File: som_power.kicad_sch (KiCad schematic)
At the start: 87 parts, among them J1 Hermaphroditic_Molex_203456-0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, Q10 DMG1012T-7, Q11 DMG1012T-7, Q17 DMG1012T-7, Q18 DMG1012T-7, Q20 DMG1012T-7, Q22 DMG1012T-7, Q7 DMG1012T-7, Q8 DMG1012T-7, SW2 SW_SPDT_PCM12SMTR, U70 MAX16150A_SOT, U72 TPS3840PL30DBVR

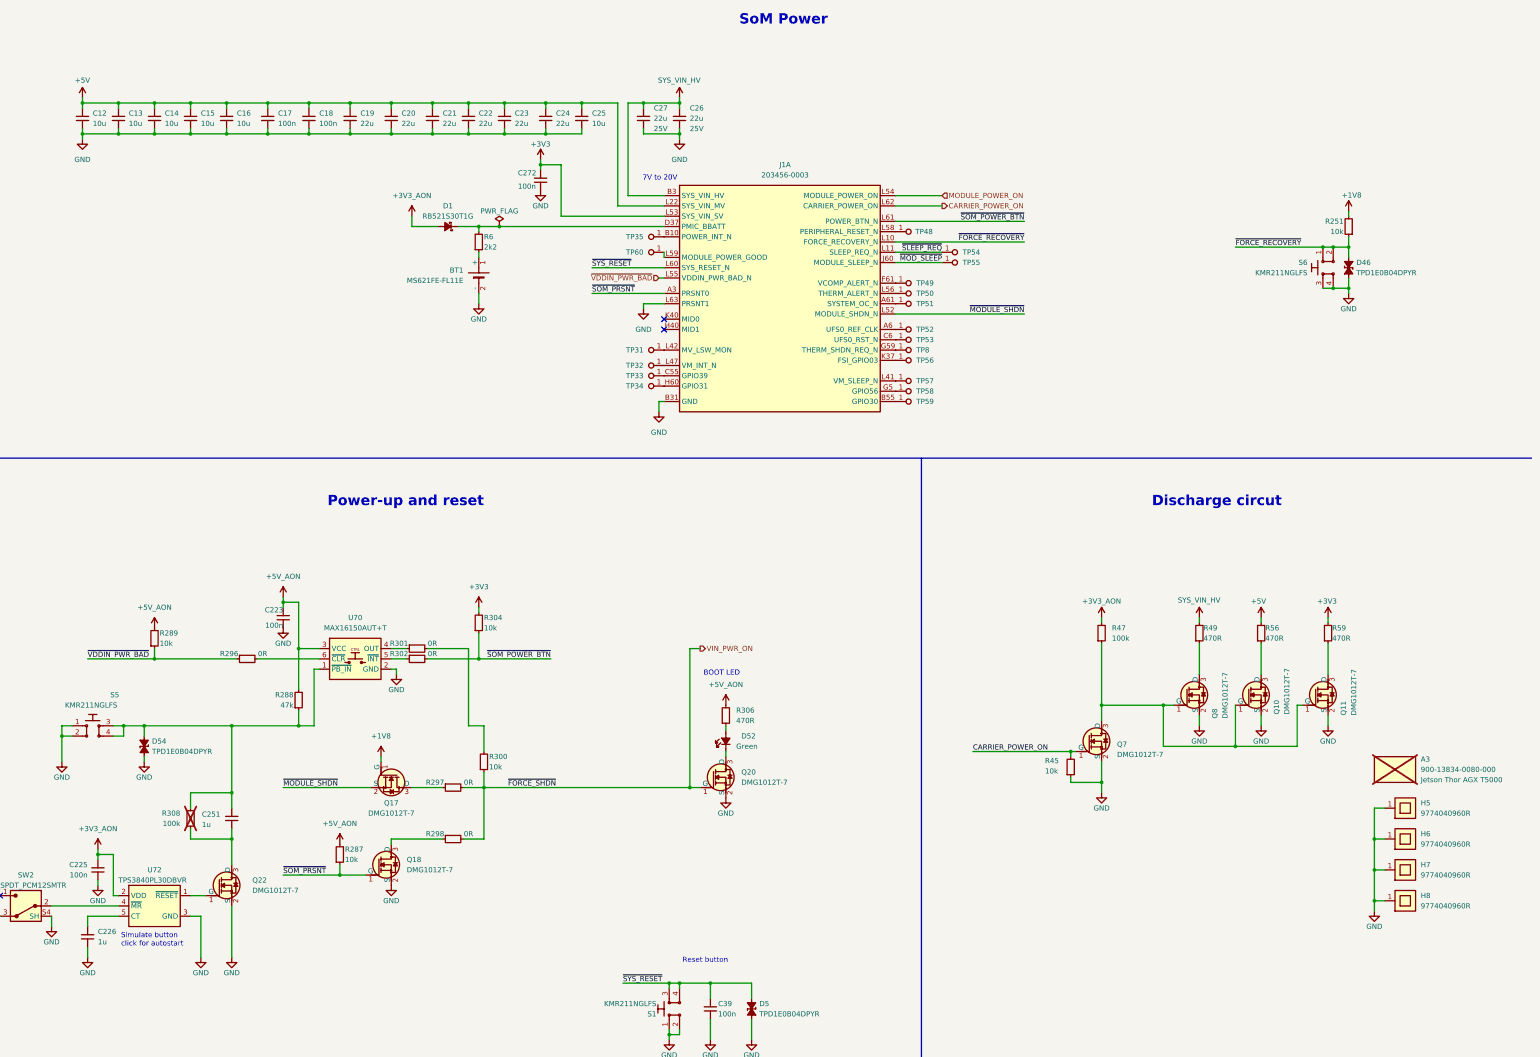
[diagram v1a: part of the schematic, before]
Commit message: [#85488] Correct Power sequence
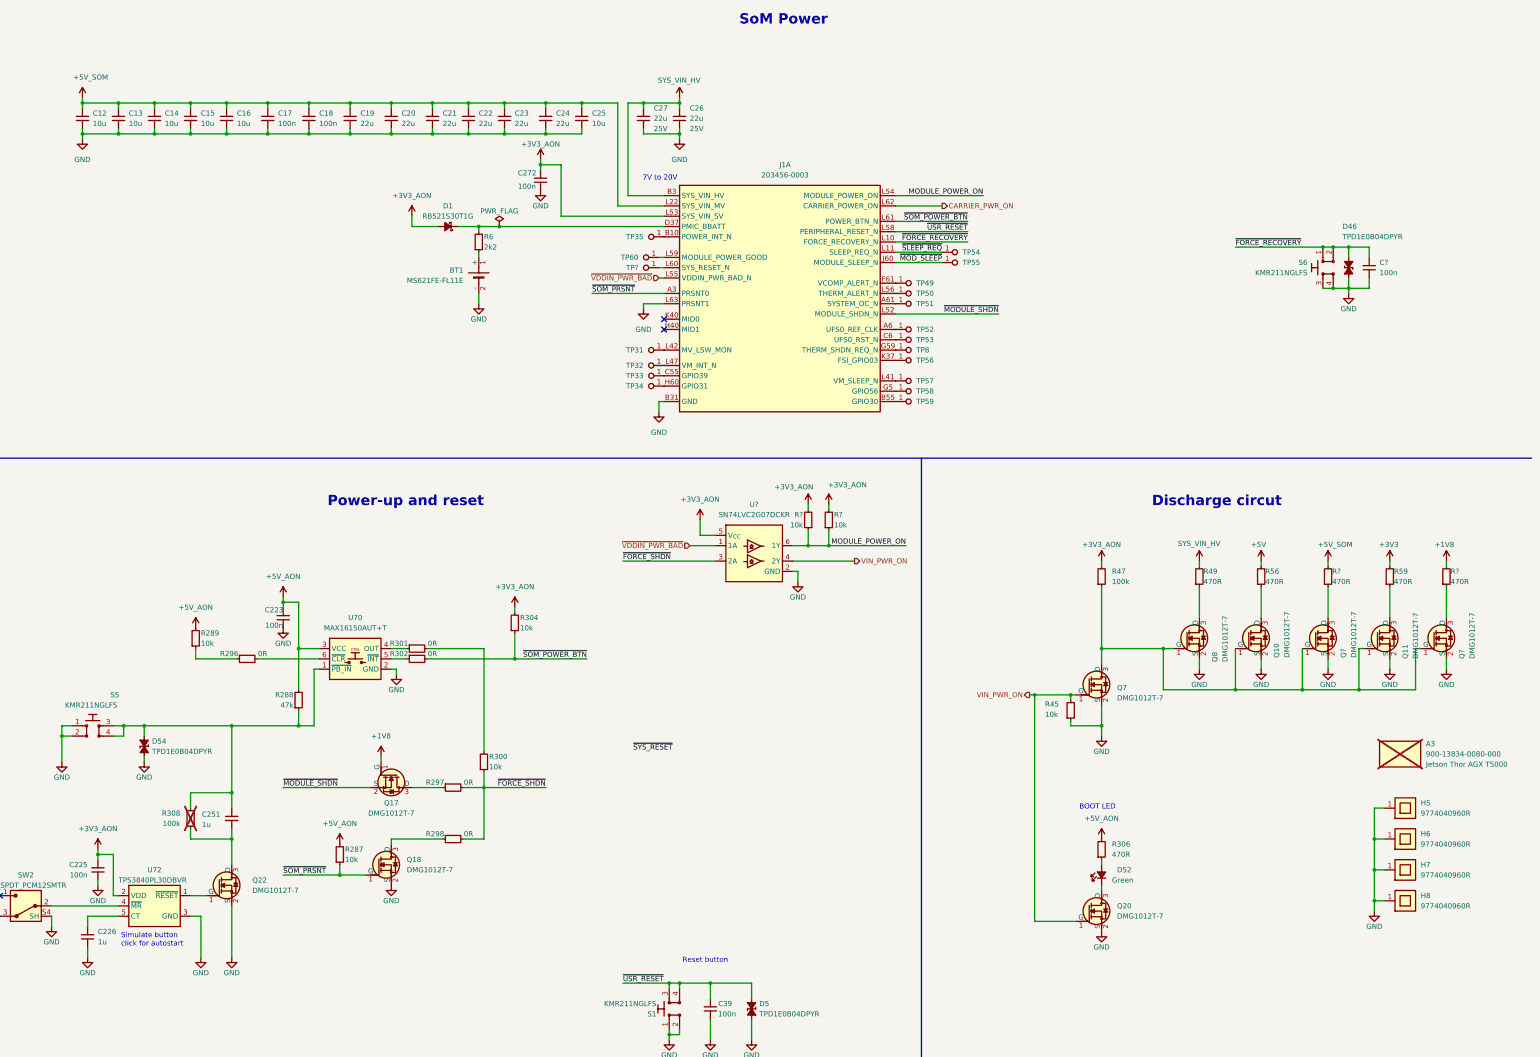
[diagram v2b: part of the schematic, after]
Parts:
- removed R251: R_10k_0402, antmicro-footprints:R_0402_1005Metric, symbol antmicroResistors0402:R_10k_0402
- removed TP48: TP_0.75mm_SMD, antmicro-footprints:TP_SMD_0.75mm, symbol antmicroTestPoints:TP_0.75mm_SMD
- added C?: C_100n_0402, antmicro-footprints:C_0402_1005Metric, symbol antmicroCapacitors0402:C_100n_0402
- added Q? (x2): DMG1012T-7, antmicro-footprints:SOT-523, symbol antmicroTransistorsFETsMOSFETsSingle:DMG1012T-7
- added R? (x2): R_10k_0402, antmicro-footprints:R_0402_1005Metric, symbol antmicroResistors0402:R_10k_0402
- added R? (x2): R_470R_0402, antmicro-footprints:R_0402_1005Metric, symbol antmicroResistors0402:R_470R_0402
- added TP?: TP_0.75mm_SMD, antmicro-footprints:TP_SMD_0.75mm, symbol antmicroTestPoints:TP_0.75mm_SMD
- added U?: SN74LVC2G07DCKR, antmicro-footprints:SC-70-6, symbol antmicroLogicBuffersDriversReceiversTransceivers:SN74LVC2G07DCKR
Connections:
- net +1V8: now also R?.2
- net +3V3: no longer C272.2, J1.L53 (SYS_VIN_SV), R304.2
- net +3V3_AON: now also C272.2, J1.L53 (SYS_VIN_SV), R304.2, R?.2, R?.2, U?.5 (V_{CC})
- net +5V: no longer C12.2, C13.2, C14.2, C15.2, C16.2, C17.2, C18.2, C19.2, C20.2, C21.2, C22.2, C23.2, C24.2, C25.2, J1.L22 (SYS_VIN_MV), J1.L23 (SYS_VIN_MV), J1.L26 (SYS_VIN_MV), J1.L27 (SYS_VIN_MV), J1.L30 (SYS_VIN_MV), J1.L31 (SYS_VIN_MV), J1.L34 (SYS_VIN_MV), J1.L35 (SYS_VIN_MV), J1.L38 (SYS_VIN_MV), J1.L39 (SYS_VIN_MV)
- net GND: now also C?.1, Q?.2 (S), Q?.2 (S), U?.2 (GND)
- net MODULE_POWER_ON: now also R?.1, R?.1, U?.6 (1Y)
- net VIN_PWR_ON: now also Q7.1 (G), R45.2, U?.4 (2Y); no longer R297.2, R298.2, R300.1
- net ~{FORCE_RECOVERY}: now also C?.2
- net ~{SYS_RESET}: no longer C39.2, D5.2 (A), J1.L60 (SYS_RESET_N), S1.3, S1.4
- net ~{VDDIN_PWR_BAD}: now also U?.1 (1A); no longer R289.1, R296.1
- net at Q10.1 (G), Q11.1 (G), Q7.3 (D)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: now also Q?.1 (G), Q?.1 (G)
- net ~{USR_RESET}: now reaches J1.L58 (PERIPHERAL_RESET_N)
- net ~{USR_RESET}: now also C39.2, D5.2 (A), S1.3, S1.4
- removed net CARRIER_POWER_ON: J1.L62 (CARRIER_POWER_ON), Q7.1 (G), R45.2
- new net: R289.1, R296.1
- new net: J1.L60 (SYS_RESET_N), TP?.1
- new net: Q?.3 (D), R?.1 (x2)
- new net +5V_SOM: C12.2, C13.2, C14.2, C15.2, C16.2, C17.2, C18.2, C19.2, C20.2, C21.2, C22.2, C23.2, C24.2, C25.2, J1.L22 (SYS_VIN_MV), J1.L23 (SYS_VIN_MV), J1.L26 (SYS_VIN_MV), J1.L27 (SYS_VIN_MV), J1.L30 (SYS_VIN_MV), J1.L31 (SYS_VIN_MV), J1.L34 (SYS_VIN_MV), J1.L35 (SYS_VIN_MV), J1.L38 (SYS_VIN_MV), J1.L39 (SYS_VIN_MV), R?.2
- new net CARRIER_PWR_ON: J1.L62 (CARRIER_POWER_ON)
- new net ~{FORCE_SHDN}: R297.2, R298.2, R300.1, U?.3 (2A)
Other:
- moved on the sheet: A3, D52, Q10, Q11, Q20, Q7, Q8, R289, R304, R306, R45, R47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

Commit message: [#85488] Sync sch branches
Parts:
- gave numbers to parts that had none: 9
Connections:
- net ~{SYS_RESET}: now also C39.2, D5.2 (A), J1.L60 (SYS_RESET_N), S1.3, S1.4
- net at TP48.1: now also J1.L58 (PERIPHERAL_RESET_N); no longer J1.L60 (SYS_RESET_N)
- removed net ~{USR_RESET}: C39.2, D5.2 (A), J1.L58 (PERIPHERAL_RESET_N), S1.3, S1.4
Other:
- moved on the sheet: TP48, TP60
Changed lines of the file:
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@@
 		)
 	)
+	(wire
+		(pts
+			(xy 194.31 78.74) (xy 194.31 80.01)
+		)
+		(stroke
+			(width 0)
+			(type default)
+		)
+	)
 	(polyline
 		(pts
@@
 	(wire
 		(pts
-			(xy 193.04 80.01) (xy 194.31 80.01)
+			(xy 193.04 78.74) (xy 194.31 78.74)
 		)
 		(stroke
@@
 	(wire
 		(pts
+			(xy 176.53 82.55) (xy 194.31 82.55)
+		)
+		(stroke
+			(width 0)
+			(type default)
+		)
+	)
+	(wire
+		(pts
 			(xy 52.07 242.57) (xy 52.07 245.11)
 		)
@@
 	(wire
 		(pts
-			(xy 193.04 82.55) (xy 194.31 82.55)
-		)
-		(stroke
-			(width 0)
-			(type default)
-		)
-	)
-	(wire
-		(pts
 			(xy 285.75 243.84) (xy 295.91 243.84)
 		)
@@
 		)
 	)
-	(label "~{USR_RESET}"
+	(label "~{SYS_RESET}"
 		(at 184.15 259.08 0)
 		(effects
@@
 	)
 	(label "~{SYS_RESET}"
-		(at 186.69 201.93 0)
+		(at 176.53 82.55 0)
 		(effects
 			(font
@@
 		)
 	)
-	(label "~{USR_RESET}"
-		(at 269.24 73.66 180)
-		(effects
-			(font
-				(size 1.27 1.27)
-			)
-			(justify right bottom)
-		)
-	)
 	(label "~{MODULE_SHDN}"
 		(at 276.86 93.98 180)
@@
 		(dnp no)
 		(fields_autoplaced yes)
-		(property "Reference" "C?"
+		(property "Reference" "C239"
 			(at 370.84 81.2736 90)
 			(effects
@@
 			(project "jetson-agx-thor-baseboard"
 				(path "/f569b0be-0afd-48b7-93ee-28582a4c645c/33df10a9-5b30-4fa6-b34e-d62ce1b48c65"
-					(reference "C?")
+					(reference "C239")
 					(unit 1)
 				)
@@
 		(on_board yes)
 		(dnp no)
-		(property "Reference" "R?"
+		(property "Reference" "R14"
 			(at 228.6 143.51 90)
 			(effects
@@
 			(project "jetson-agx-thor-baseboard"
 				(path "/f569b0be-0afd-48b7-93ee-28582a4c645c/33df10a9-5b30-4fa6-b34e-d62ce1b48c65"
-					(reference "R?")
+					(reference "R14")
 					(unit 1)
 				)
@@
 		(dnp no)
 		(fields_autoplaced yes)
-		(property "Reference" "U?"
+		(property "Reference" "U74"
 			(at 216.535 140.97 0)
 			(effects
@@
 			(project "jetson-agx-thor-baseboard"
 				(path "/f569b0be-0afd-48b7-93ee-28582a4c645c/33df10a9-5b30-4fa6-b34e-d62ce1b48c65"
-					(reference "U?")
+					(reference "U74")
 					(unit 1)
 				)
@@
 	(symbol
 		(lib_id "antmicroTestPoints:TP_0.75mm_SMD")
-		(at 193.04 82.55 0)
-		(mirror y)
+		(at 269.24 73.66 0)
 		(unit 1)
 		(exclude_from_sim no)
@@
 		(on_board yes)
 		(dnp no)
-		(fields_autoplaced yes)
-		(property "Reference" "TP?"
-			(at 187.96 82.55 0)
+		(property "Reference" "TP48"
+			(at 274.32 73.66 0)
 			(effects
 				(font
@@
 		)
 		(property "Value" "TP_0.75mm_SMD"
-			(at 182.88 86.36 0)
+			(at 279.4 77.47 0)
 			(effects
 				(font
@@
 		)
 		(property "Footprint" "antmicro-footprints:TP_SMD_0.75mm"
-			(at 182.88 88.9 0)
+			(at 279.4 80.01 0)
 			(effects
 				(font
@@
 		)
 		(property "Datasheet" ""
-			(at 175.26 95.25 0)
+			(at 287.02 86.36 0)
 			(effects
 				(font
@@
 		)
 		(property "Description" "SMT test point"
-			(at 193.04 82.55 0)
+			(at 269.24 73.66 0)
 			(effects
 				(font
@@
 		)
 		(property "MPN" ""
-			(at 182.245 93.98 0)
+			(at 280.035 85.09 0)
 			(effects
 				(font
@@
 		)
 		(property "Manufacturer" ""
-			(at 182.245 88.9 0)
+			(at 280.035 80.01 0)
 			(effects
 				(font
@@
 		)
 		(property "Author" "Antmicro"
-			(at 182.88 91.44 0)
+			(at 279.4 82.55 0)
 			(effects
 				(font
@@
 		)
 		(property "License" "Apache-2.0"
-			(at 182.88 93.98 0)
+			(at 279.4 85.09 0)
 			(effects
 				(font
@@
 			(project "jetson-agx-thor-baseboard"
 				(path "/f569b0be-0afd-48b7-93ee-28582a4c645c/33df10a9-5b30-4fa6-b34e-d62ce1b48c65"
-					(reference "TP?")
+					(reference "TP48")
 					(unit 1)
 				)
@@
 	(symbol
 		(lib_id "antmicroTestPoints:TP_0.75mm_SMD")
-		(at 193.04 80.01 0)
+		(at 193.04 78.74 0)
 		(mirror y)
 		(unit 1)
@@
 		(fields_autoplaced yes)
 		(property "Reference" "TP60"
-			(at 187.96 80.01 0)
+			(at 187.96 78.74 0)
 			(effects
 				(font
@@
 		)
 		(property "Value" "TP_0.75mm_SMD"
-			(at 182.88 83.82 0)
+			(at 182.88 82.55 0)
 			(effects
 				(font
@@
 		)
 		(property "Footprint" "antmicro-footprints:TP_SMD_0.75mm"
-			(at 182.88 86.36 0)
+			(at 182.88 85.09 0)
 			(effects
 				(font
@@
 		)
 		(property "Datasheet" ""
-			(at 175.26 92.71 0)
+			(at 175.26 91.44 0)
 			(effects
 				(font
@@
 		)
 		(property "Description" "SMT test point"
-			(at 193.04 80.01 0)
+			(at 193.04 78.74 0)
 			(effects
 				(font
@@
 		)
 		(property "MPN" ""
-			(at 182.245 91.44 0)
+			(at 182.245 90.17 0)
 			(effects
 				(font
@@
 		)
 		(property "Manufacturer" ""
-			(at 182.245 86.36 0)
+			(at 182.245 85.09 0)
 			(effects
 				(font
@@
 		)
 		(property "Author" "Antmicro"
-			(at 182.88 88.9 0)
+			(at 182.88 87.63 0)
 			(effects
 				(font
@@
 		)
 		(property "License" "Apache-2.0"
-			(at 182.88 91.44 0)
+			(at 182.88 90.17 0)
 			(effects
 				(font
@@
 		(on_board yes)
 		(dnp no)
-		(property "Reference" "R?"
+		(property "Reference" "R50"
 			(at 359.156 157.48 90)
 			(effects
@@
 			(project "jetson-agx-thor-baseboard"
 				(path "/f569b0be-0afd-48b7-93ee-28582a4c645c/33df10a9-5b30-4fa6-b34e-d62ce1b48c65"
-					(reference "R?")
+					(reference "R50")
 					(unit 1)
 				)
@@
 		(on_board yes)
 		(dnp no)
-		(property "Reference" "Q?"
+		(property "Reference" "Q38"
 			(at 391.16 179.07 90)
 			(effects
@@
 			(project "jetson-agx-thor-baseboard"
 				(path "/f569b0be-0afd-48b7-93ee-28582a4c645c/33df10a9-5b30-4fa6-b34e-d62ce1b48c65"
-					(reference "Q?")
+					(reference "Q38")
 					(unit 1)
 				)
@@
 		(on_board yes)
 		(dnp no)
-		(property "Reference" "R?"
+		(property "Reference" "R24"
 			(at 236.22 143.51 90)
 			(effects
@@
 			(project "jetson-agx-thor-baseboard"
 				(path "/f569b0be-0afd-48b7-93ee-28582a4c645c/33df10a9-5b30-4fa6-b34e-d62ce1b48c65"
-					(reference "R?")
+					(reference "R24")
 					(unit 1)
 				)
@@
 		(on_board yes)
 		(dnp no)
-		(property "Reference" "R?"
+		(property "Reference" "R60"
 			(at 388.366 157.48 90)
 			(effects
@@
 			(project "jetson-agx-thor-baseboard"
 				(path "/f569b0be-0afd-48b7-93ee-28582a4c645c/33df10a9-5b30-4fa6-b34e-d62ce1b48c65"
-					(reference "R?")
+					(reference "R60")
 					(unit 1)
 				)
@@
 		(on_board yes)
 		(dnp no)
-		(property "Reference" "Q?"
+		(property "Reference" "Q37"
 			(at 361.95 178.816 90)
 			(effects
@@
 			(project "jetson-agx-thor-baseboard"
 				(path "/f569b0be-0afd-48b7-93ee-28582a4c645c/33df10a9-5b30-4fa6-b34e-d62ce1b48c65"
-					(reference "Q?")
+					(reference "Q37")
 					(unit 1)
 				)
